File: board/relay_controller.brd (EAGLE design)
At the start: 60 x 65 mm, 78 parts, among them IC1 STM32F103C8T, IC3 AT24C, K1 G6K-2F-Y, K2 G6K-2F-Y, K3 G6K-2F-Y, K7 G6K-2F-Y, K8 G6K-2F-Y, Q1 220mA/50V/3.5Ω, Q2 220mA/50V/3.5Ω, Q3 220mA/50V/3.5Ω, Q4 220mA/50V/3.5Ω, Q5 220mA/50V/3.5Ω

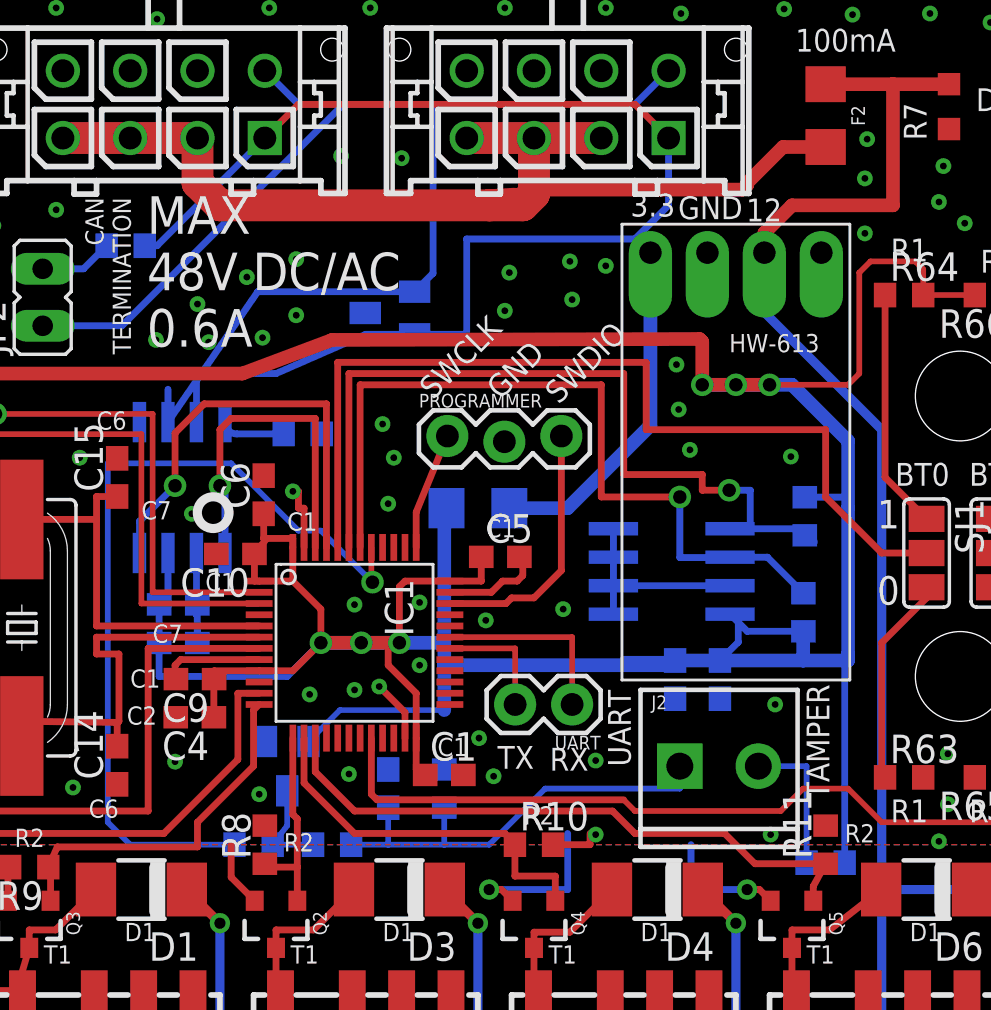
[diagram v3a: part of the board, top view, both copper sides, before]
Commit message: DRC check fixes
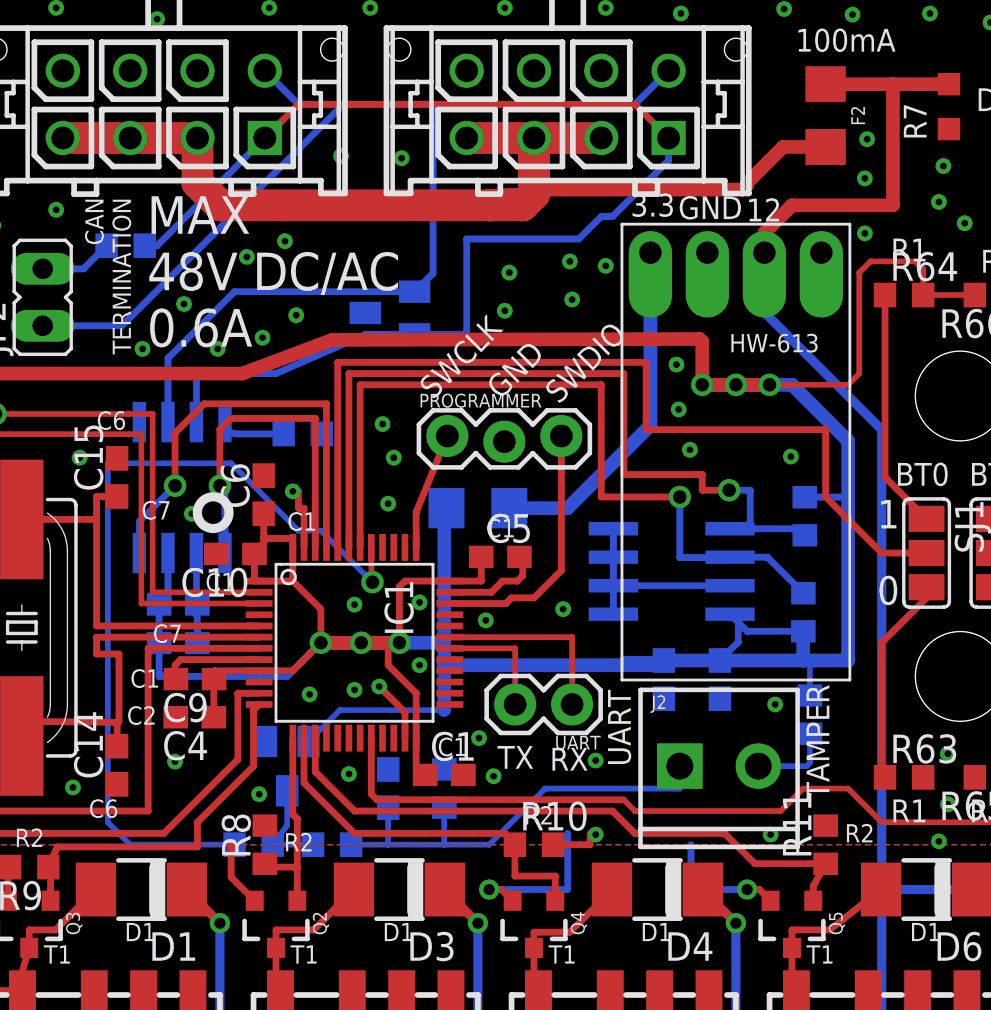
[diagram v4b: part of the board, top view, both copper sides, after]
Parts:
- moved R60 6.64 mm to (48.3, 30.8), turned to 90 degrees
- moved C2 0.50 mm to (41.8, 32.4)
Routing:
- net +3V3: track 212.6 -> 205.3 mm
- net N$10: track 6.45 -> 3.66 mm
- net CAN_H: track 58.0 -> 56.9 mm
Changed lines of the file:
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@@
 <elements>
 <element name="IC1" library="micro-stm" package="LQFP48" value="STM32F103C8T" x="28" y="34" rot="R270"/>
-<element name="C2" library="rcl" package="C0603" value="1u" x="42.29" y="32.36" rot="MR270"/>
+<element name="C2" library="rcl" package="C0603" value="1u" x="41.79" y="32.36" rot="MR270"/>
 <element name="C3" library="rcl" package="C0603" value="100n" x="20.14" y="33.99" rot="MR180"/>
 <element name="C4" library="rcl" package="C0603" value="1u" x="20.88" y="30.68" rot="R180"/>
@@
 </element>
 <element name="D18" library="diode" package="SOT23" value="BAS70-04" x="25" y="28.5" rot="MR180"/>
-<element name="R60" library="rcl" package="R0603" value="100" x="49" y="24.2" rot="MR180"/>
+<element name="R60" library="rcl" package="R0603" value="100" x="48.3" y="30.8" rot="MR90"/>
 <element name="R61" library="rcl" package="R0603" value="100" x="23.5" y="25" rot="MR0"/>
 <element name="R62" library="rcl" package="R0603" value="1k" x="27" y="25" rot="MR0"/>
@@
 <via x="29.75" y="42.25" extent="1-16" drill="0.3"/>
 <via x="29.25" y="43.75" extent="1-16" drill="0.3"/>
-<via x="19.15" y="47.5" extent="1-16" drill="0.3"/>
-<via x="21.5" y="47.4" extent="1-16" drill="0.3"/>
+<via x="18.55" y="47.1" extent="1-16" drill="0.3"/>
+<via x="21.9" y="47.1" extent="1-16" drill="0.3"/>
 <via x="4.9" y="28.55" extent="1-16" drill="0.3"/>
 <contactref element="S2" pad="1"/>
@@
 <via x="14.7" y="62.3" extent="1-16" drill="0.3"/>
 <via x="10.8" y="54.1" extent="1-16" drill="0.3"/>
-<via x="25.4" y="51.1" extent="1-16" drill="0.3"/>
+<via x="24.9" y="51.9" extent="1-16" drill="0.3"/>
 <via x="14.7" y="53.3" extent="1-16" drill="0.3"/>
-<via x="23.2" y="50.3" extent="1-16" drill="0.3"/>
-<via x="21" y="49.1" extent="1-16" drill="0.3"/>
+<via x="23.2" y="51.2" extent="1-16" drill="0.3"/>
+<via x="20.4" y="49.1" extent="1-16" drill="0.3"/>
 <via x="27.4" y="55.7" extent="1-16" drill="0.3"/>
 <via x="30.1" y="55.6" extent="1-16" drill="0.3"/>
@@
 <wire x1="19.685" y1="37.5" x2="19.685" y2="35.605" width="0.3048" layer="16"/>
 <wire x1="19.685" y1="35.605" x2="19.29" y2="35.71" width="0.3048" layer="16"/>
-<wire x1="40" y1="33.21" x2="42.29" y2="33.21" width="0.4064" layer="16"/>
+<wire x1="40" y1="33.21" x2="41.79" y2="33.21" width="0.4064" layer="16"/>
 <wire x1="19.29" y1="33.99" x2="19.29" y2="35.71" width="0.3048" layer="16"/>
 <wire x1="19.685" y1="37.5" x2="19.685" y2="38.0025" width="0.4064" layer="16"/>
@@
 <wire x1="25.95" y1="29.6" x2="27.35" y2="31" width="0.254" layer="16"/>
 <wire x1="27.35" y1="31" x2="32" y2="31" width="0.254" layer="16"/>
-<wire x1="42.29" y1="33.21" x2="42.09" y2="33" width="0.3048" layer="16"/>
+<wire x1="41.79" y1="33.21" x2="42.09" y2="33" width="0.3048" layer="16"/>
 <wire x1="42.09" y1="33" x2="42" y2="33" width="0.3048" layer="16"/>
 <via x="45" y="45.5" extent="1-16" drill="0.6"/>
@@
 <wire x1="43.376703125" y1="47.540940625" x2="43.5" y2="47.41764375" width="0.6096" layer="1"/>
 <wire x1="43.5" y1="47.41764375" x2="43.5" y2="45.5" width="0.6096" layer="1"/>
-<wire x1="42.29" y1="33.21" x2="44.29" y2="33.21" width="0.6096" layer="16"/>
+<wire x1="41.79" y1="33.21" x2="44.29" y2="33.21" width="0.6096" layer="16"/>
 <wire x1="44.29" y1="33.21" x2="48" y2="33.21" width="0.6096" layer="16"/>
 <wire x1="48" y1="33.21" x2="48" y2="34.5" width="0.6096" layer="16"/>
-<wire x1="48" y1="33.21" x2="50" y2="33.21" width="0.6096" layer="16"/>
+<wire x1="48" y1="33.21" x2="48.5" y2="33.21" width="0.6096" layer="16"/>
+<wire x1="48.5" y1="33.21" x2="50" y2="33.21" width="0.6096" layer="16"/>
 <wire x1="50" y1="33.21" x2="50" y2="33.5" width="0.6096" layer="16"/>
 <wire x1="50" y1="33.5" x2="50" y2="40" width="0.6096" layer="16"/>
@@
 <wire x1="50.5" y1="46" x2="50" y2="45.5" width="0.254" layer="1"/>
 <wire x1="50" y1="45.5" x2="46.5" y2="45.5" width="0.254" layer="1"/>
-<wire x1="49.85" y1="24.2" x2="49.85" y2="33.35" width="0.3048" layer="16"/>
 <wire x1="49.85" y1="33.35" x2="50" y2="33.5" width="0.3048" layer="16"/>
+<wire x1="48.3" y1="31.65" x2="48.3" y2="33.21" width="0.254" layer="16"/>
+<wire x1="48.3" y1="33.21" x2="48.5" y2="33.21" width="0.254" layer="16"/>
 </signal>
 <signal name="RELAY_16">
@@
 <contactref element="X4" pad="P$1"/>
 <contactref element="X3" pad="P$1"/>
-<wire x1="42" y1="56.5" x2="42" y2="53.5" width="0.3048" layer="16"/>
 <wire x1="24" y1="56.5" x2="25.5" y2="58" width="0.3048" layer="1"/>
 <wire x1="25.5" y1="58" x2="40.5" y2="58" width="0.3048" layer="1"/>
@@
 <contactref element="R25" pad="2"/>
 <wire x1="18.65" y1="51.7" x2="19.2" y2="51.7" width="0.3048" layer="16"/>
-<wire x1="42" y1="53.5" x2="40.5" y2="52" width="0.3048" layer="16"/>
-<wire x1="40.5" y1="52" x2="33" y2="52" width="0.3048" layer="16"/>
 <wire x1="33" y1="52" x2="33" y2="47.75" width="0.3048" layer="16"/>
 <wire x1="33" y1="47.75" x2="30.68" y2="47.75" width="0.3048" layer="16"/>
 <wire x1="30.68" y1="47.75" x2="28.5" y2="47.75" width="0.3048" layer="16"/>
 <wire x1="28.5" y1="47.75" x2="24.5" y2="46" width="0.3048" layer="16"/>
+<wire x1="33" y1="52" x2="38" y2="52" width="0.3048" layer="16"/>
+<wire x1="38" y1="52" x2="39" y2="53" width="0.3048" layer="16"/>
+<wire x1="39" y1="53" x2="39.5" y2="53" width="0.3048" layer="16"/>
+<wire x1="39.5" y1="53" x2="42" y2="55.5" width="0.3048" layer="16"/>
+<wire x1="42" y1="55.5" x2="42" y2="56.5" width="0.3048" layer="16"/>
 </signal>
 <signal name="CAN_L">
 <contactref element="DA1" pad="6"/>
 <contactref element="D5" pad="1"/>
-<wire x1="19.685" y1="43.8375" x2="19.685" y2="45.3" width="0.3048" layer="16"/>
-<wire x1="23.685" y1="49.65" x2="19.685" y2="43.8375" width="0.3048" layer="16"/>
 <contactref element="X4" pad="P$5"/>
 <contactref element="X3" pad="P$5"/>
@@
 <wire x1="30.68" y1="49.65" x2="31.5" y2="50.47" width="0.3048" layer="16"/>
 <wire x1="31.5" y1="50.47" x2="31.5" y2="58" width="0.3048" layer="16"/>
-<wire x1="23.685" y1="49.65" x2="30.68" y2="49.65" width="0.3048" layer="16"/>
+<wire x1="22.65" y1="49.65" x2="30.68" y2="49.65" width="0.3048" layer="16"/>
+<wire x1="19.685" y1="43.8375" x2="19.685" y2="46.685" width="0.3048" layer="16"/>
+<wire x1="19.685" y1="46.685" x2="22.65" y2="49.65" width="0.3048" layer="16"/>
 </signal>
 <signal name="N$17">
@@
 <signal name="N$10">
 <contactref element="R60" pad="1"/>
-<wire x1="48.15" y1="24.2" x2="48.15" y2="28.5" width="0.254" layer="16"/>
 <contactref element="J2" pad="2"/>
 <wire x1="46" y1="28.5" x2="48.15" y2="28.5" width="0.254" layer="16"/>
+<wire x1="48.15" y1="28.5" x2="48.3" y2="28.65" width="0.254" layer="16"/>
+<wire x1="48.3" y1="28.65" x2="48.3" y2="29.95" width="0.254" layer="16"/>
 </signal>
 <signal name="N$5">
@@
 </signal>
 </signals>
+<errors>
+</errors>
 </board>
 </drawing>
